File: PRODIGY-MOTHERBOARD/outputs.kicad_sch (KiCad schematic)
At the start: 8 parts, among them J10 SERIAL, J3 GPIO, J4 PWM_OUT, J5 A_IN, J6 MOTOR, J7 SPI_OUT, J8 I2C, J9 CAN

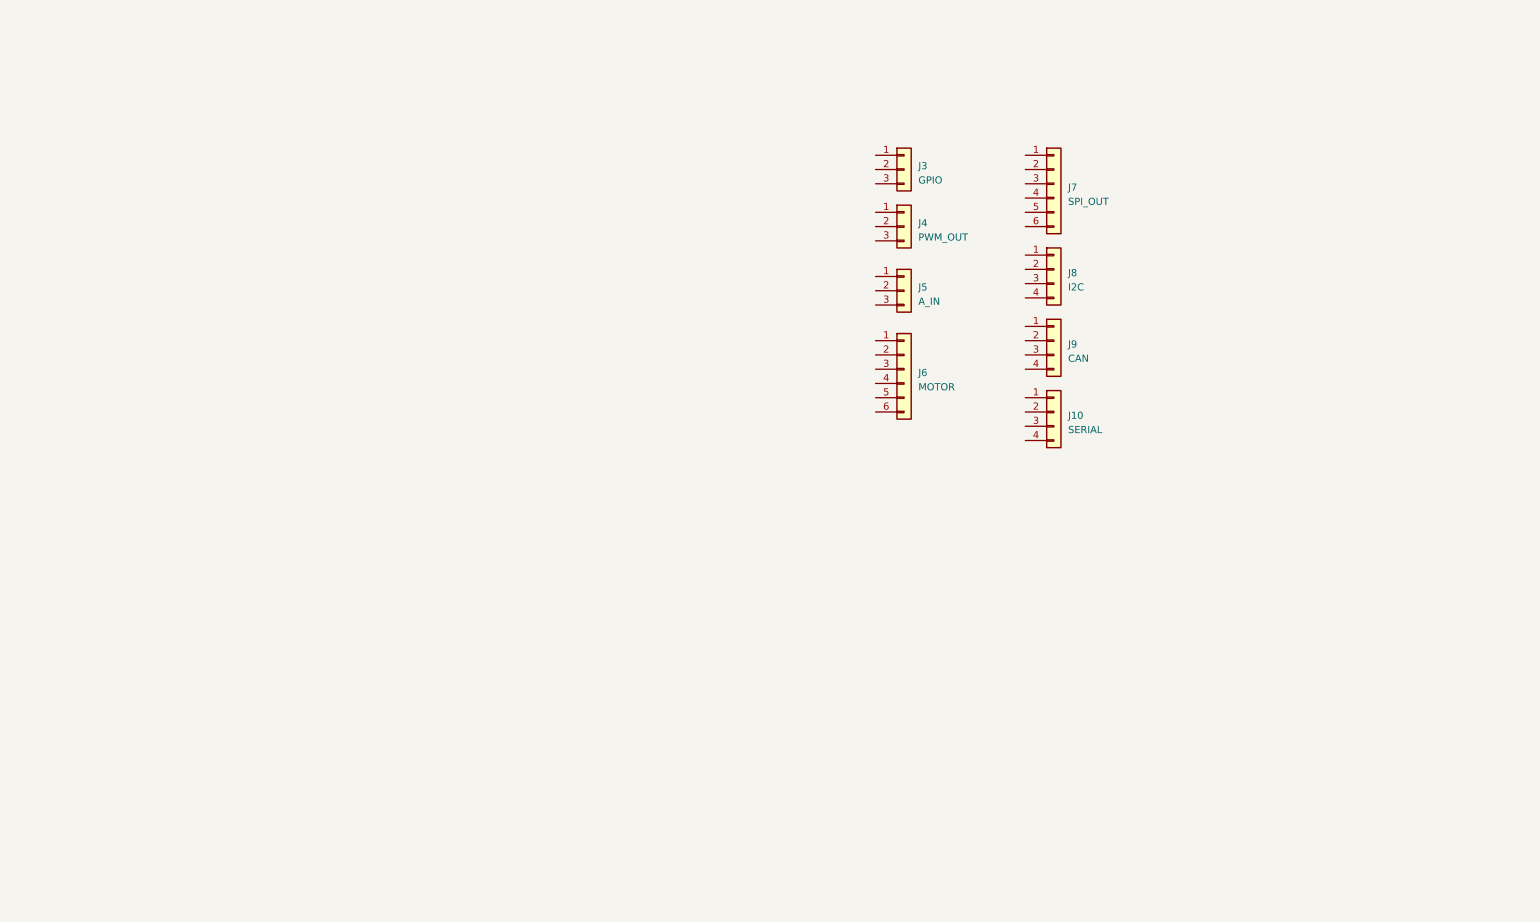
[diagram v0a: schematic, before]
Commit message: project restructure done. Hierarchical sheet done. Outputs/breakouts sheet done
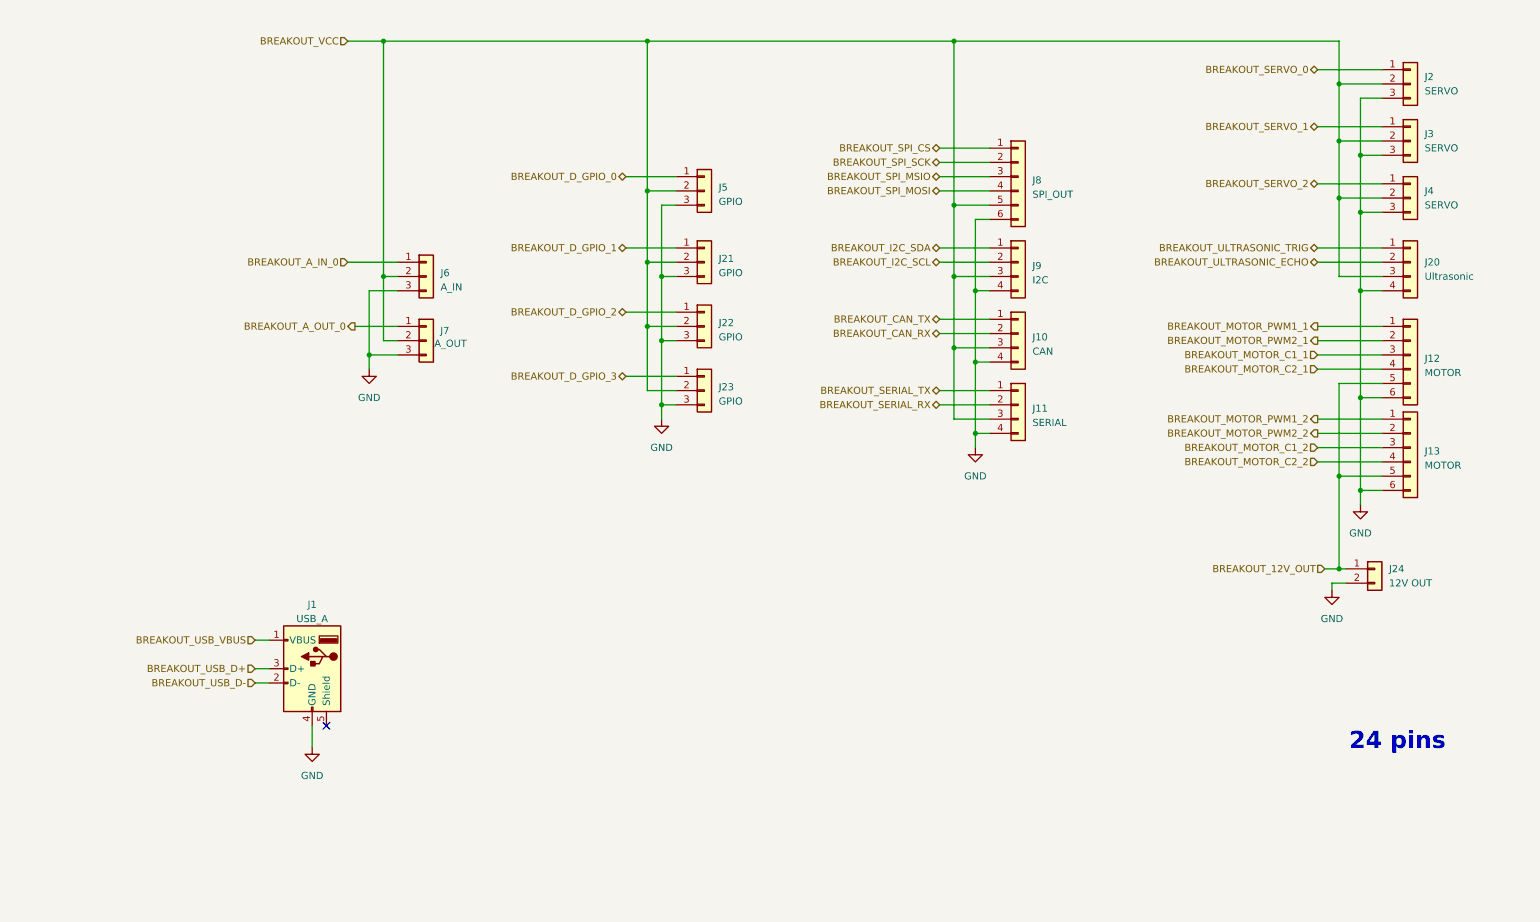
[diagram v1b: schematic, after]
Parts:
- added J1: USB_A, Connector_USB:USB_A_TE_292303-7_Horizontal, symbol Connector:USB_A
- added J13: MOTOR, Connector_JST:JST_XH_S6B-XH-A_1x06_P2.50mm_Horizontal, symbol Connector_Generic:Conn_01x06
- added J20: Ultrasonic, Connector_JST:JST_XH_S4B-XH-A_1x04_P2.50mm_Horizontal, symbol Connector_Generic:Conn_01x04
- added J21, J22, J23, J5: GPIO, Connector_JST:JST_XH_S3B-XH-A_1x03_P2.50mm_Horizontal, symbol Connector_Generic:Conn_01x03
- added J24: 12V OUT, TerminalBlock_Phoenix:TerminalBlock_Phoenix_MKDS-1,5-2-5.08_1x02_P5.08mm_Horizontal, symbol Connector_Generic:Conn_01x02
- added J3: SERVO, Connector_JST:JST_XH_S3B-XH-A_1x03_P2.50mm_Horizontal, symbol Connector_Generic:Conn_01x03
- added J7: A_OUT, Connector_JST:JST_XH_S3B-XH-A_1x03_P2.50mm_Horizontal, symbol Connector_Generic:Conn_01x03
- J2: renamed from J3; value GPIO -> SERVO
- J4: value PWM_OUT -> SERVO
- renumbered J9 to J10, J10 to J11, J6 to J12, J5 to J6, J7 to J8, J8 to J9
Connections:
- net BREAKOUT_MOTOR_PWM1_1: now reaches J12.1 (Pin_1)
- net BREAKOUT_MOTOR_PWM2_1: now reaches J12.2 (Pin_2)
- net BREAKOUT_MOTOR_C1_1: now reaches J12.3 (Pin_3)
- net BREAKOUT_MOTOR_C2_1: now reaches J12.4 (Pin_4)
- net BREAKOUT_12V_OUT: now reaches J12.5 (Pin_5)
- net BREAKOUT_12V_OUT: now also J13.5 (Pin_5), J24.1 (Pin_1)
- net GND: now reaches J12.6 (Pin_6)
- net GND: now also J10.4 (Pin_4), J11.4 (Pin_4), J2.3 (Pin_3), J4.3 (Pin_3), J6.3 (Pin_3), J8.6 (Pin_6), J9.4 (Pin_4), J1.4 (GND), J13.6 (Pin_6), J20.4 (Pin_4), J21.3 (Pin_3), J22.3 (Pin_3), J23.3 (Pin_3), J24.2 (Pin_2), J3.3 (Pin_3), J5.3 (Pin_3), J7.3 (Pin_3)
- net BREAKOUT_I2C_SDA: now reaches J9.1 (Pin_1)
- net BREAKOUT_I2C_SCL: now reaches J9.2 (Pin_2)
- net BREAKOUT_VCC: now reaches J9.3 (Pin_3)
- net BREAKOUT_VCC: now also J10.3 (Pin_3), J11.3 (Pin_3), J2.2 (Pin_2), J4.2 (Pin_2), J6.2 (Pin_2), J8.5 (Pin_5), J20.3 (Pin_3), J21.2 (Pin_2), J22.2 (Pin_2), J23.2 (Pin_2), J3.2 (Pin_2), J5.2 (Pin_2), J7.2 (Pin_2)
- net BREAKOUT_SERVO_0: now reaches J2.1 (Pin_1)
- net BREAKOUT_A_IN_0: now reaches J6.1 (Pin_1)
- net BREAKOUT_SERVO_2: now reaches J4.1 (Pin_1)
- net BREAKOUT_CAN_TX: now reaches J10.1 (Pin_1)
- net BREAKOUT_CAN_RX: now reaches J10.2 (Pin_2)
- net BREAKOUT_SPI_CS: now reaches J8.1 (Pin_1)
- net BREAKOUT_SPI_SCK: now reaches J8.2 (Pin_2)
- net BREAKOUT_SPI_MSIO: now reaches J8.3 (Pin_3)
- net BREAKOUT_SPI_MOSI: now reaches J8.4 (Pin_4)
- net BREAKOUT_SERIAL_TX: now reaches J11.1 (Pin_1)
- net BREAKOUT_SERIAL_RX: now reaches J11.2 (Pin_2)
- new net BREAKOUT_A_OUT_0: J7.1 (Pin_1)
- new net BREAKOUT_D_GPIO_0: J5.1 (Pin_1)
- new net BREAKOUT_D_GPIO_1: J21.1 (Pin_1)
- new net BREAKOUT_D_GPIO_2: J22.1 (Pin_1)
- new net BREAKOUT_D_GPIO_3: J23.1 (Pin_1)
- new net BREAKOUT_MOTOR_C1_2: J13.3 (Pin_3)
- new net BREAKOUT_MOTOR_C2_2: J13.4 (Pin_4)
- new net BREAKOUT_MOTOR_PWM1_2: J13.1 (Pin_1)
- new net BREAKOUT_MOTOR_PWM2_2: J13.2 (Pin_2)
- new net BREAKOUT_SERVO_1: J3.1 (Pin_1)
- new net BREAKOUT_ULTRASONIC_ECHO: J20.2 (Pin_2)
- new net BREAKOUT_ULTRASONIC_TRIG: J20.1 (Pin_1)
- new net BREAKOUT_USB_D+: J1.3 (D+)
- new net BREAKOUT_USB_D-: J1.2 (D-)
- new net BREAKOUT_USB_VBUS: J1.1 (VBUS)
- no-connect marks 0 -> 1
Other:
- note added: "24 pins"
- moved on the sheet: J10, J11, J12, J2, J6, J8, J9

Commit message: Finished I2C device and bus schematics. Added logic level translation.
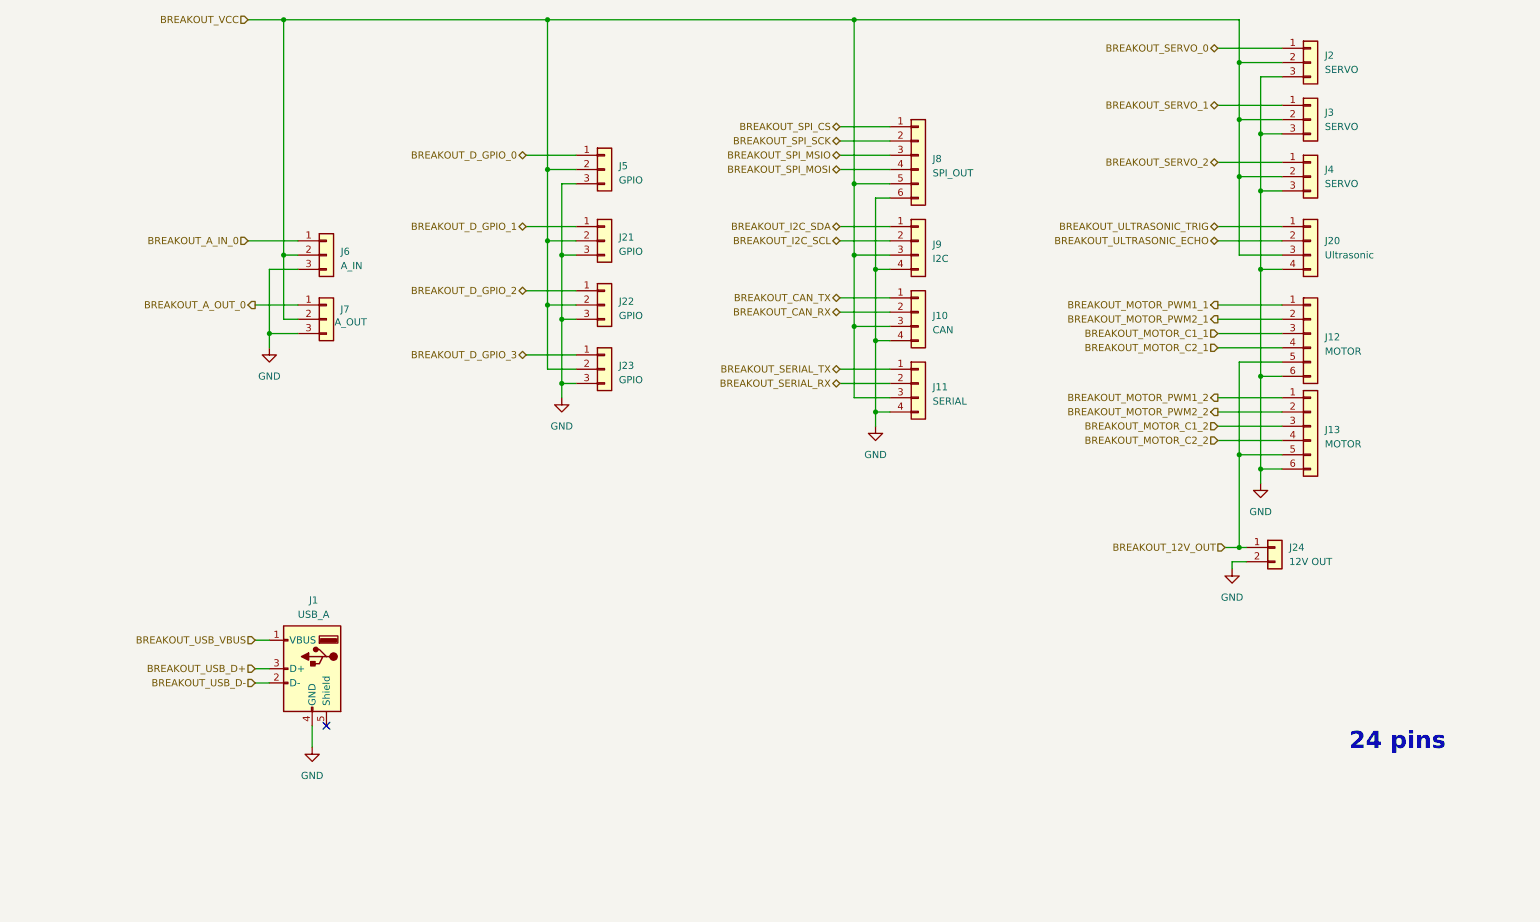
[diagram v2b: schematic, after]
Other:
- moved on the sheet: J10, J11, J12, J13, J2, J20, J21, J22, J23, J24, J3, J4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

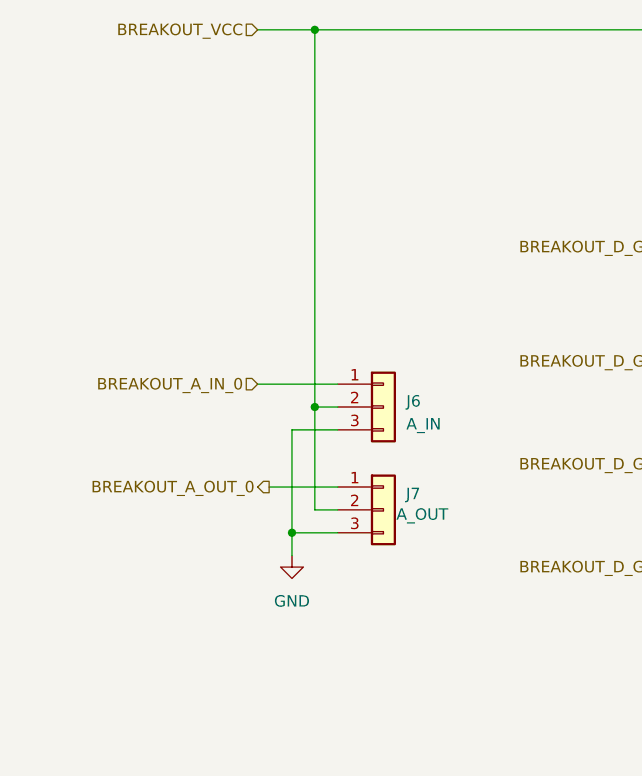
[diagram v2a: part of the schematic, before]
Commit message: SPI SD CARD circuit added.
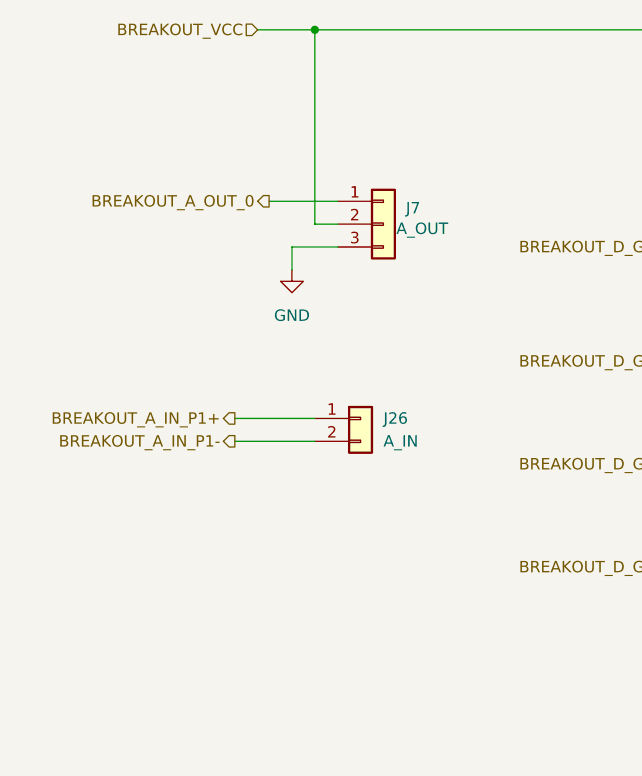
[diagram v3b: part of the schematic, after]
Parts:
- removed J6: A_IN, Connector_JST:JST_XH_S3B-XH-A_1x03_P2.50mm_Horizontal, symbol Connector_Generic:Conn_01x03
- added J26: A_IN, Connector_JST:JST_XH_S3B-XH-A_1x02_P2.50mm_Horizontal, symbol Connector_Generic:Conn_01x02
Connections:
- new net BREAKOUT_A_IN_P1+: J26.1 (Pin_1)
- new net BREAKOUT_A_IN_P1-: J26.2 (Pin_2)
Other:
- moved on the sheet: J7
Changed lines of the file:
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@@
 	)
 	(junction
-		(at 64.77 69.85)
-		(diameter 0)
-		(color 0 0 0 0)
-	)
-	(junction
 		(at 166.37 69.85)
 		(diameter 0)
@@
 	)
 	(junction
-		(at 62.23 83.82)
-		(diameter 0)
-		(color 0 0 0 0)
-	)
-	(junction
 		(at 114.3 69.85)
 		(diameter 0)
@@
 	(wire
 		(pts
-			(xy 64.77 69.85) (xy 67.31 69.85)
-		)
-		(stroke
-			(width 0)
-			(type default)
-		)
-	)
-	(wire
-		(pts
 			(xy 107.95 87.63) (xy 116.84 87.63)
 		)
@@
 	(wire
 		(pts
-			(xy 59.69 78.74) (xy 67.31 78.74)
+			(xy 59.69 46.99) (xy 67.31 46.99)
 		)
 		(stroke
@@
 	(wire
 		(pts
-			(xy 62.23 83.82) (xy 62.23 86.36)
-		)
-		(stroke
-			(width 0)
-			(type default)
-		)
-	)
-	(wire
-		(pts
-			(xy 62.23 72.39) (xy 67.31 72.39)
+			(xy 62.23 52.07) (xy 62.23 54.61)
 		)
 		(stroke
@@
 	(wire
 		(pts
-			(xy 64.77 27.94) (xy 64.77 69.85)
-		)
-		(stroke
-			(width 0)
-			(type default)
-		)
-	)
-	(wire
-		(pts
 			(xy 238.76 91.44) (xy 238.76 107.95)
 		)
@@
 	(wire
 		(pts
-			(xy 67.31 81.28) (xy 64.77 81.28)
+			(xy 67.31 49.53) (xy 64.77 49.53)
 		)
 		(stroke
@@
 	(wire
 		(pts
+			(xy 55.88 73.66) (xy 64.77 73.66)
+		)
+		(stroke
+			(width 0)
+			(type default)
+		)
+	)
+	(wire
+		(pts
 			(xy 111.76 78.74) (xy 116.84 78.74)
 		)
@@
 	(wire
 		(pts
-			(xy 62.23 72.39) (xy 62.23 83.82)
-		)
-		(stroke
-			(width 0)
-			(type default)
-		)
-	)
-	(wire
-		(pts
 			(xy 231.14 43.18) (xy 242.57 43.18)
 		)
@@
 	(wire
 		(pts
-			(xy 62.23 83.82) (xy 67.31 83.82)
+			(xy 62.23 52.07) (xy 67.31 52.07)
 		)
 		(stroke
@@
 	(wire
 		(pts
-			(xy 58.42 67.31) (xy 67.31 67.31)
+			(xy 55.88 71.12) (xy 64.77 71.12)
 		)
 		(stroke
@@
 	(wire
 		(pts
-			(xy 64.77 69.85) (xy 64.77 81.28)
+			(xy 64.77 27.94) (xy 64.77 49.53)
 		)
 		(stroke
@@
 	(hierarchical_label "BREAKOUT_A_OUT_0"
 		(shape output)
-		(at 59.69 78.74 180)
+		(at 59.69 46.99 180)
 		(fields_autoplaced yes)
 		(effects
@@
 		)
 	)
-	(hierarchical_label "BREAKOUT_A_IN_0"
-		(shape input)
-		(at 58.42 67.31 180)
+	(hierarchical_label "BREAKOUT_A_IN_P1+"
+		(shape output)
+		(at 55.88 71.12 180)
 		(fields_autoplaced yes)
 		(effects
@@
 		)
 	)
+	(hierarchical_label "BREAKOUT_A_IN_P1-"
+		(shape output)
+		(at 55.88 73.66 180)
+		(fields_autoplaced yes)
+		(effects
+			(font
+				(size 1.27 1.27)
+			)
+			(justify right)
+		)
+	)
 	(symbol
 		(lib_id "Connector_Generic:Conn_01x06")
@@
 	(symbol
 		(lib_id "Connector_Generic:Conn_01x03")
-		(at 72.39 81.28 0)
+		(at 72.39 49.53 0)
 		(unit 1)
 		(exclude_from_sim no)
@@
 		(dnp no)
 		(property "Reference" "J7"
-			(at 75.692 79.502 0)
+			(at 75.692 47.752 0)
 			(effects
 				(font
@@
 		)
 		(property "Value" "A_OUT"
-			(at 76.708 81.788 0)
+			(at 76.708 50.038 0)
 			(effects
 				(font
@@
 		)
 		(property "Footprint" "Connector_JST:JST_XH_S3B-XH-A_1x03_P2.50mm_Horizontal"
-			(at 72.39 81.28 0)
+			(at 72.39 49.53 0)
 			(effects
 				(font
@@
 		)
 		(property "Datasheet" "~"
-			(at 72.39 81.28 0)
+			(at 72.39 49.53 0)
 			(effects
 				(font
@@
 		)
 		(property "Description" ""
-			(at 72.39 81.28 0)
+			(at 72.39 49.53 0)
 			(effects
 				(font
@@
 		)
 		(property "JLCPCB" ""
-			(at 72.39 81.28 0)
+			(at 72.39 49.53 0)
 			(effects
 				(font
@@
 	)
 	(symbol
-		(lib_id "Connector_Generic:Conn_01x03")
-		(at 72.39 69.85 0)
-		(unit 1)
-		(exclude_from_sim no)
-		(in_bom yes)
-		(on_board yes)
-		(dnp no)
-		(fields_autoplaced yes)
-		(property "Reference" "J6"
-			(at 74.93 69.215 0)
-			(effects
-				(font
-					(size 1.27 1.27)
-				)
-				(justify left)
-			)
-		)
-		(property "Value" "A_IN"
-			(at 74.93 71.755 0)
-			(effects
-				(font
-					(size 1.27 1.27)
-				)
-				(justify left)
-			)
-		)
-		(property "Footprint" "Connector_JST:JST_XH_S3B-XH-A_1x03_P2.50mm_Horizontal"
-			(at 72.39 69.85 0)
-			(effects
-				(font
-					(size 1.27 1.27)
-				)
-				(hide yes)
-			)
-		)
-		(property "Datasheet" "~"
-			(at 72.39 69.85 0)
-			(effects
-				(font
-					(size 1.27 1.27)
-				)
-				(hide yes)
-			)
-		)
-		(property "Description" ""
-			(at 72.39 69.85 0)
-			(effects
-				(font
-					(size 1.27 1.27)
-				)
-				(hide yes)
-			)
-		)
-		(property "JLCPCB" ""
-			(at 72.39 69.85 0)
-			(effects
-				(font
-					(size 1.27 1.27)
-				)
-				(hide yes)
-			)
-		)
-		(pin "1"
-		)
-		(pin "2"
-		)
-		(pin "3"
-		)
-		(instances
-			(project "PRODIGY-MOTHERBOARD"
-				(path "/f1c25860-8989-4190-bd24-2491d23ca7d9/a962dcec-9dee-4e54-acaa-e8da87dab487"
-					(reference "J6")
-					(unit 1)
-				)
-			)
-		)
-	)
-	(symbol
 		(lib_id "Connector_Generic:Conn_01x02")
 		(at 241.3 121.92 0)
@@
 	)
 	(symbol
+		(lib_id "Connector_Generic:Conn_01x02")
+		(at 69.85 71.12 0)
+		(unit 1)
+		(exclude_from_sim no)
+		(in_bom yes)
+		(on_board yes)
+		(dnp no)
+		(fields_autoplaced yes)
+		(property "Reference" "J26"
+			(at 72.39 71.1199 0)
+			(effects
+				(font
+					(size 1.27 1.27)
+				)
+				(justify left)
+			)
+		)
+		(property "Value" "A_IN"
+			(at 72.39 73.6599 0)
+			(effects
+				(font
+					(size 1.27 1.27)
+				)
+				(justify left)
+			)
+		)
+		(property "Footprint" "Connector_JST:JST_XH_S3B-XH-A_1x02_P2.50mm_Horizontal"
+			(at 69.85 71.12 0)
+			(effects
+				(font
+					(size 1.27 1.27)
+				)
+				(hide yes)
+			)
+		)
+		(property "Datasheet" "~"
+			(at 69.85 71.12 0)
+			(effects
+				(font
+					(size 1.27 1.27)
+				)
+				(hide yes)
+			)
+		)
+		(property "Description" "Generic connector, single row, 01x02, script generated (kicad-library-utils/schlib/autogen/connector/)"
+			(at 69.85 71.12 0)
+			(effects
+				(font
+					(size 1.27 1.27)
+				)
+				(hide yes)
+			)
+		)
+		(pin "2"
+		)
+		(pin "1"
+		)
+		(instances
+			(project "PRODIGY-MOTHERBOARD"
+				(path "/f1c25860-8989-4190-bd24-2491d23ca7d9/a962dcec-9dee-4e54-acaa-e8da87dab487"
+					(reference "J26")
+					(unit 1)
+				)
+			)
+		)
+	)
+	(symbol
 		(lib_id "Connector_Generic:Conn_01x03")
 		(at 121.92 67.31 0)
@@
 	(symbol
 		(lib_id "power:GND")
-		(at 62.23 86.36 0)
+		(at 62.23 54.61 0)
 		(unit 1)
 		(exclude_from_sim no)
@@
 		(fields_autoplaced yes)
 		(property "Reference" "#PWR027"
-			(at 62.23 92.71 0)
+			(at 62.23 60.96 0)
 			(effects
 				(font
@@
 		)
 		(property "Value" "GND"
-			(at 62.23 91.44 0)
+			(at 62.23 59.69 0)
 			(effects
 				(font
@@
 		)
 		(property "Footprint" ""
-			(at 62.23 86.36 0)
+			(at 62.23 54.61 0)
 			(effects
 				(font
@@
 		)
 		(property "Datasheet" ""
-			(at 62.23 86.36 0)
+			(at 62.23 54.61 0)
 			(effects
 				(font
@@
 		)
 		(property "Description" "Power symbol creates a global label with name \"GND\" , ground"
-			(at 62.23 86.36 0)
+			(at 62.23 54.61 0)
 			(effects
 				(font

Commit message: CAN schematic done
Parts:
- added J6: Neopixel, Connector_JST:JST_XH_S3B-XH-A_1x03_P2.50mm_Horizontal, symbol Connector_Generic:Conn_01x03
- J16: renamed from J2; now not fitted
- J17: renamed from J3; now not fitted
- J18: renamed from J4; now not fitted
- J19: renamed from J20; now not fitted
- renumbered J23 to J10, J8 to J11, J9 to J12, J10 to J13, J11 to J14, J24 to J15, J12 to J20, J13 to J21, J26 to J3, J1 to J4, J7 to J5, J5 to J7, J21 to J8, J22 to J9
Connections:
- net BREAKOUT_VCC: now also J6.2 (Pin_2)
- net GND: now also J6.3 (Pin_3)
- net BREAKOUT_CAN_RX renamed BREAKOUT_CAN_L
- net BREAKOUT_CAN_TX renamed BREAKOUT_CAN_H
- new net BREAKOUT_NEOPIXEL_IN: J6.1 (Pin_1)
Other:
- moved on the sheet: J11, J12, J13, J14, J3
